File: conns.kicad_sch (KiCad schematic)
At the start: 10 parts, among them J1 GSB1C4621DS1HR, J2 M20-8770546 (for SWD), J3 M20-8770342 (for RasPi), J4 JST-XH, J6 SMA_CONNECTOR, J7 SMA_CONNECTOR

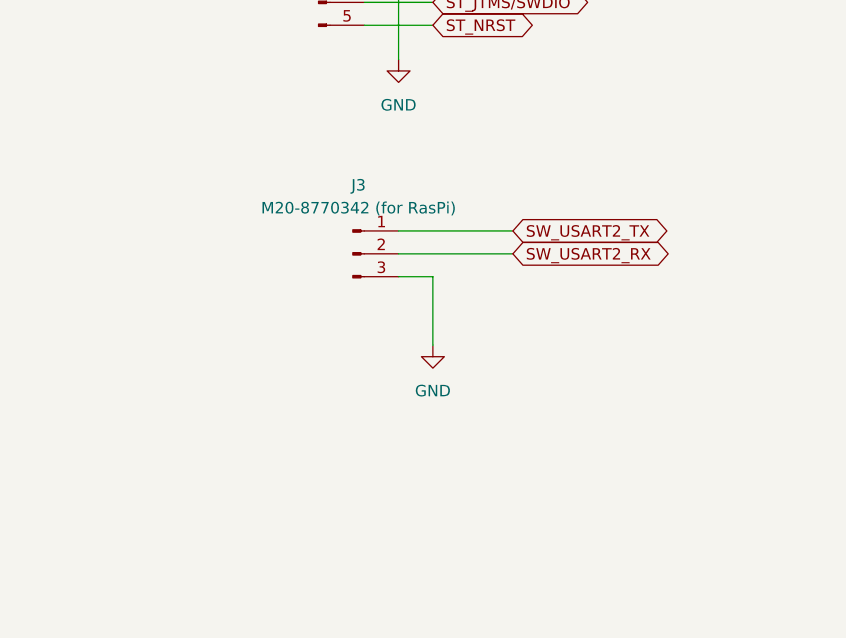
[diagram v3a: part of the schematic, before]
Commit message: adding connectors for display and pi power, pin headers
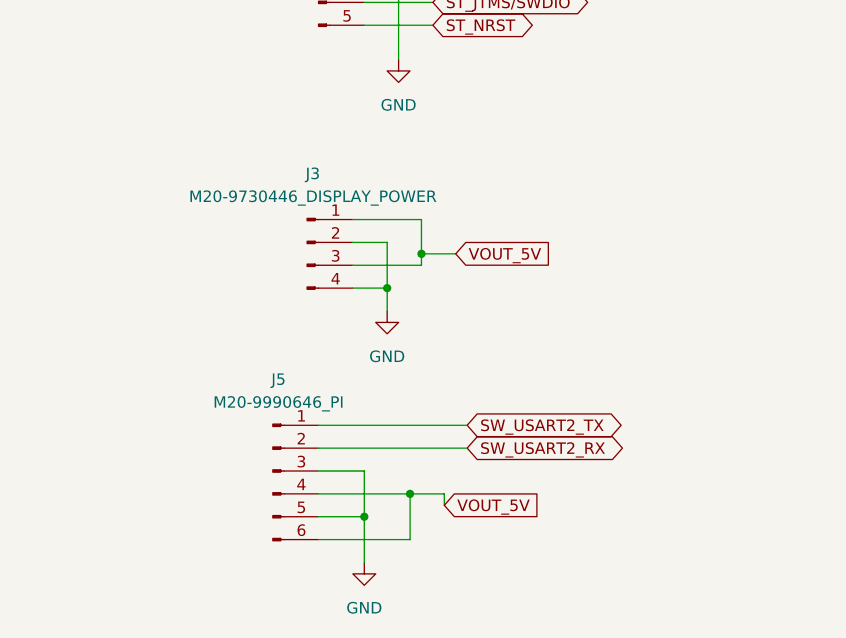
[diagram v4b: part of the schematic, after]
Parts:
- removed J3: M20-8770342 (for RasPi), Connector_PinSocket_2.54mm:PinSocket_1x03_P2.54mm_Vertical, symbol Connector:Conn_01x03_Pin
- added J3: M20-9730446_DISPLAY_POWER, Connector_PinHeader_2.54mm:PinHeader_1x04_P2.54mm_Vertical, symbol Connector:Conn_01x04_Pin
- added J5: M20-9990646_PI, Connector_PinHeader_2.54mm:PinHeader_1x06_P2.54mm_Vertical, symbol Connector:Conn_01x06_Pin
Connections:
- net GND: now also J3.2 (Pin_2), J3.4 (Pin_4), J5.3 (Pin_3), J5.5 (Pin_5)
- net SW_USART2_RX: now also J5.2 (Pin_2)
- net SW_USART2_TX: now also J5.1 (Pin_1)
- new net VOUT_5V: J3.1 (Pin_1), J3.3 (Pin_3), J5.4 (Pin_4), J5.6 (Pin_6)

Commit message: adding the .stp files for 3d viewer
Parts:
- J2: footprint Connector_PinSocket_2.54mm:PinSocket_1x05_P2.54mm_Vertical -> Connector_PinHeader_2.54mm:PinHeader_1x05_P2.54mm_Vertical
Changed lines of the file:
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@@
       (effects (font (size 1.27 1.27)))
     )
-    (property "Footprint" "Connector_PinSocket_2.54mm:PinSocket_1x05_P2.54mm_Vertical" (at 50.8 111.76 0)
+    (property "Footprint" "Connector_PinHeader_2.54mm:PinHeader_1x05_P2.54mm_Vertical" (at 50.8 111.76 0)
       (effects (font (size 1.27 1.27)) hide)
     )

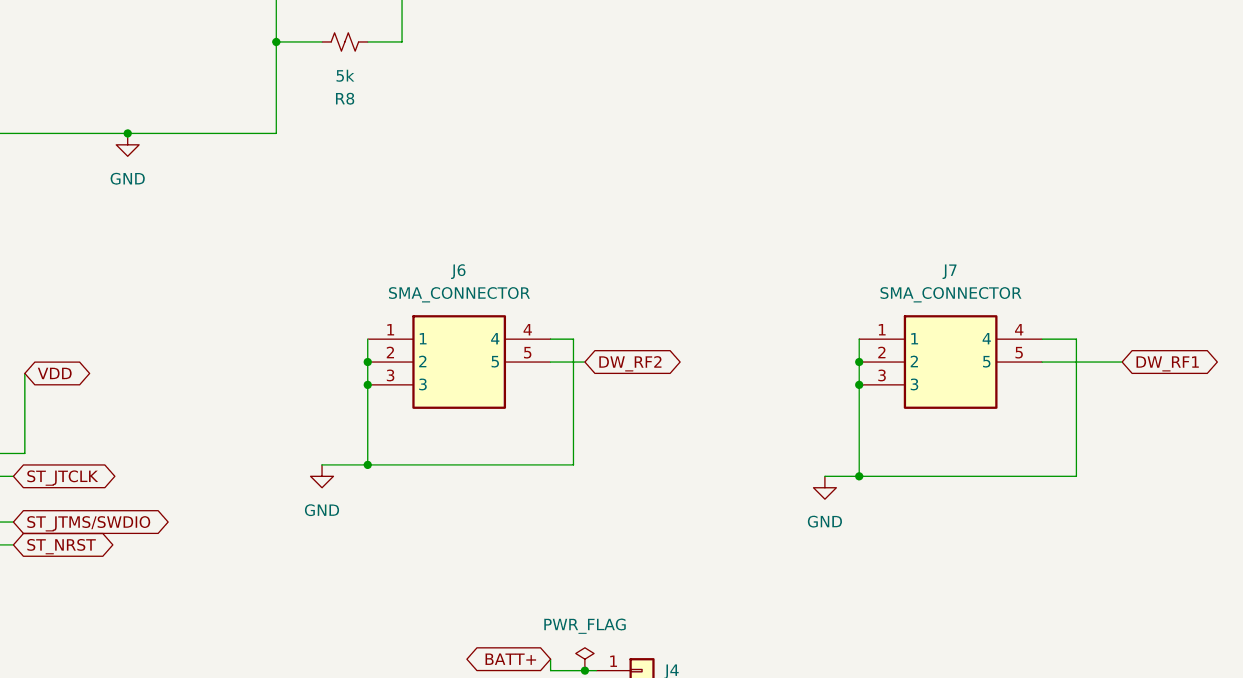
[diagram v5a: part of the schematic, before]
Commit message: routing on rf ic DW3220
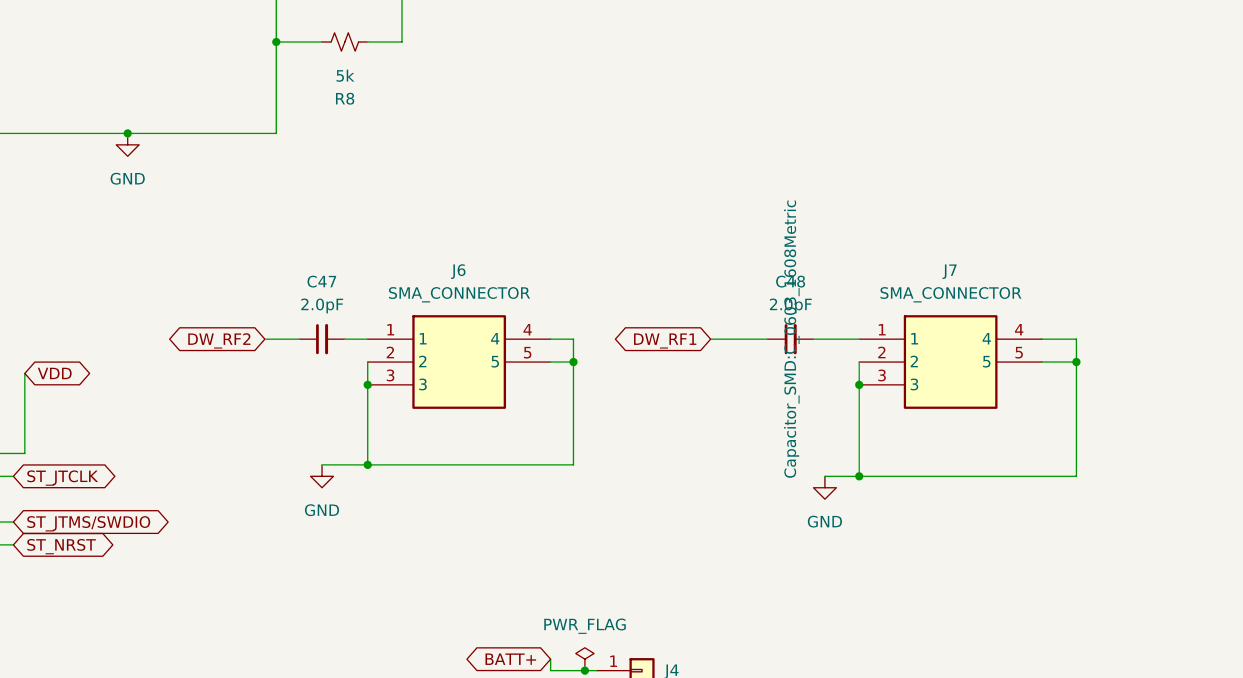
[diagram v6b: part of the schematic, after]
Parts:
- added C47, C48: 2.0pF, Capacitor_SMD:C_0603_1608Metric, symbol Device:C_Small
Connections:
- net DW_RF1: now also C48.1; no longer J7.5
- net DW_RF2: now also C47.1; no longer J6.5
- net GND: now also J6.5, J7.5; no longer J6.1, J7.1
- new net: C47.2, J6.1
- new net: C48.2, J7.1
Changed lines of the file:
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@@
   (junction (at 58.42 146.05) (diameter 0) (color 0 0 0 0)
   )
+  (junction (at 181.61 96.52) (diameter 0) (color 0 0 0 0)
+  )
+  (junction (at 125.73 96.52) (diameter 0) (color 0 0 0 0)
+  )
   (junction (at 92.71 60.96) (diameter 0) (color 0 0 0 0)
   )
   (junction (at 102.87 99.06) (diameter 0) (color 0 0 0 0)
   )
-  (junction (at 102.87 96.52) (diameter 0) (color 0 0 0 0)
-  )
   (junction (at 62.23 142.24) (diameter 0) (color 0 0 0 0)
   )
@@
   )
   (junction (at 92.71 53.34) (diameter 0) (color 0 0 0 0)
-  )
-  (junction (at 157.48 96.52) (diameter 0) (color 0 0 0 0)
   )
   (junction (at 60.96 168.91) (diameter 0) (color 0 0 0 0)
@@
     (stroke (width 0) (type default))
   )
-  (wire (pts (xy 102.87 93.98) (xy 102.87 96.52))
-    (stroke (width 0) (type default))
-  )
-  (wire (pts (xy 123.19 96.52) (xy 127 96.52))
-    (stroke (width 0) (type default))
-  )
   (wire (pts (xy 90.17 53.34) (xy 92.71 53.34))
     (stroke (width 0) (type default))
   )
+  (wire (pts (xy 181.61 96.52) (xy 181.61 109.22))
+    (stroke (width 0) (type default))
+  )
   (wire (pts (xy 62.23 143.51) (xy 62.23 142.24))
     (stroke (width 0) (type default))
   )
+  (wire (pts (xy 123.19 96.52) (xy 125.73 96.52))
+    (stroke (width 0) (type default))
+  )
   (wire (pts (xy 50.8 166.37) (xy 55.88 166.37))
     (stroke (width 0) (type default))
@@
     (stroke (width 0) (type default))
   )
+  (wire (pts (xy 125.73 96.52) (xy 125.73 107.95))
+    (stroke (width 0) (type default))
+  )
   (wire (pts (xy 64.77 106.68) (xy 64.77 97.79))
     (stroke (width 0) (type default))
@@
     (stroke (width 0) (type default))
   )
-  (wire (pts (xy 181.61 93.98) (xy 181.61 109.22))
+  (wire (pts (xy 152.4 93.98) (xy 157.48 93.98))
+    (stroke (width 0) (type default))
+  )
+  (wire (pts (xy 181.61 93.98) (xy 181.61 96.52))
     (stroke (width 0) (type default))
   )
@@
     (stroke (width 0) (type default))
   )
-  (wire (pts (xy 186.69 96.52) (xy 177.8 96.52))
-    (stroke (width 0) (type default))
-  )
   (wire (pts (xy 58.42 140.97) (xy 58.42 146.05))
     (stroke (width 0) (type default))
@@
     (stroke (width 0) (type default))
   )
-  (wire (pts (xy 157.48 93.98) (xy 157.48 96.52))
+  (wire (pts (xy 100.33 93.98) (xy 102.87 93.98))
     (stroke (width 0) (type default))
   )
@@
     (stroke (width 0) (type default))
   )
+  (wire (pts (xy 91.44 93.98) (xy 95.25 93.98))
+    (stroke (width 0) (type default))
+  )
   (wire (pts (xy 39.37 50.8) (xy 39.37 53.34))
     (stroke (width 0) (type default))
@@
     (stroke (width 0) (type default))
   )
+  (wire (pts (xy 140.97 93.98) (xy 147.32 93.98))
+    (stroke (width 0) (type default))
+  )
   (wire (pts (xy 50.8 163.83) (xy 67.31 163.83))
     (stroke (width 0) (type default))
@@
     (stroke (width 0) (type default))
   )
-  (wire (pts (xy 125.73 93.98) (xy 125.73 107.95))
+  (wire (pts (xy 125.73 93.98) (xy 125.73 96.52))
+    (stroke (width 0) (type default))
+  )
+  (wire (pts (xy 177.8 96.52) (xy 181.61 96.52))
     (stroke (width 0) (type default))
   )
@@
     )
   )
+  (global_label "DW_RF2" (shape bidirectional) (at 91.44 93.98 180) (fields_autoplaced)
+    (effects (font (size 1.27 1.27)) (justify right))
+    (property "Intersheetrefs" "${INTERSHEET_REFS}" (at 80.0864 93.98 0)
+      (effects (font (size 1.27 1.27)) (justify right) hide)
+    )
+  )
   (global_label "BATT+" (shape bidirectional) (at 123.19 129.54 180) (fields_autoplaced)
     (effects (font (size 1.27 1.27)) (justify right))
@@
     )
   )
-  (global_label "DW_RF1" (shape bidirectional) (at 186.69 96.52 0) (fields_autoplaced)
-    (effects (font (size 1.27 1.27)) (justify left))
-    (property "Intersheetrefs" "${INTERSHEET_REFS}" (at 198.0436 96.52 0)
-      (effects (font (size 1.27 1.27)) (justify left) hide)
-    )
-  )
   (global_label "ST_JTCLK" (shape bidirectional) (at 63.5 109.22 0) (fields_autoplaced)
     (effects (font (size 1.27 1.27)) (justify left))
@@
     )
   )
+  (global_label "DW_RF1" (shape bidirectional) (at 140.97 93.98 180) (fields_autoplaced)
+    (effects (font (size 1.27 1.27)) (justify right))
+    (property "Intersheetrefs" "${INTERSHEET_REFS}" (at 129.6164 93.98 0)
+      (effects (font (size 1.27 1.27)) (justify right) hide)
+    )
+  )
   (global_label "SW_USART2_RX" (shape bidirectional) (at 67.31 163.83 0) (fields_autoplaced)
     (effects (font (size 1.27 1.27)) (justify left))
@@
     )
   )
-  (global_label "DW_RF2" (shape bidirectional) (at 127 96.52 0) (fields_autoplaced)
-    (effects (font (size 1.27 1.27)) (justify left))
-    (property "Intersheetrefs" "${INTERSHEET_REFS}" (at 138.3536 96.52 0)
-      (effects (font (size 1.27 1.27)) (justify left) hide)
-    )
-  )
   (symbol (lib_id "Connector:Conn_01x06_Pin") (at 45.72 166.37 0) (unit 1)
     (in_bom yes) (on_board yes) (dnp no) (fields_autoplaced)
@@
     )
   )
+  (symbol (lib_id "Device:C_Small") (at 97.79 93.98 90) (unit 1)
+    (in_bom yes) (on_board yes) (dnp no) (fields_autoplaced)
+    (property "Reference" "C47" (at 97.7963 87.63 90)
+      (effects (font (size 1.27 1.27)))
+    )
+    (property "Value" "2.0pF" (at 97.7963 90.17 90)
+      (effects (font (size 1.27 1.27)))
+    )
+    (property "Footprint" "Capacitor_SMD:C_0603_1608Metric" (at 97.79 93.98 0)
+      (effects (font (size 1.27 1.27)) hide)
+    )
+    (property "Datasheet" "~" (at 97.79 93.98 0)
+      (effects (font (size 1.27 1.27)) hide)
+    )
+    (pin "2")
+    (pin "1")
+    (instances
+      (project "radar2"
+        (path "/4b235fed-a05d-46ae-99fd-4a907d865754/dfc10a02-f047-425a-8f9d-e4a822e029f8"
+          (reference "C47") (unit 1)
+        )
+      )
+    )
+  )
   (symbol (lib_id "Connector_Generic:Conn_01x02") (at 133.35 130.81 0) (unit 1)
     (in_bom yes) (on_board yes) (dnp no) (fields_autoplaced)
@@
         )
       )
+    )
+  )
+  (symbol (lib_id "Device:C_Small") (at 149.86 93.98 90) (unit 1)
+    (in_bom yes) (on_board yes) (dnp no) (fields_autoplaced)
+    (property "Reference" "C48" (at 149.8663 87.63 90)
+      (effects (font (size 1.27 1.27)))
+    )
+    (property "Value" "2.0pF" (at 149.8663 90.17 90)
+      (effects (font (size 1.27 1.27)))
+    )
+    (property "Footprint" "Capacitor_SMD:C_0603_1608Metric" (at 149.86 93.98 0)
+      (effects (font (size 1.27 1.27)))
+    )
+    (property "Datasheet" "~" (at 149.86 93.98 0)
+      (effects (font (size 1.27 1.27)) hide)
+    )
+    (pin "2")
+    (pin "1")
+    (instances
+      (project "radar2"
+        (path "/4b235fed-a05d-46ae-99fd-4a907d865754/dfc10a02-f047-425a-8f9d-e4a822e029f8"
+          (reference "C48") (unit 1)
+        )
+      )

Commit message: changing sizes of caps from 06 to 04, also using vias on DW spi interfact to stm32
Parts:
- C47, C48: footprint Capacitor_SMD:C_0603_1608Metric -> Capacitor_SMD:C_0402_1005Metric
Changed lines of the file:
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@@
       (effects (font (size 1.27 1.27)))
     )
-    (property "Footprint" "Capacitor_SMD:C_0603_1608Metric" (at 97.79 93.98 0)
+    (property "Footprint" "Capacitor_SMD:C_0402_1005Metric" (at 97.79 93.98 0)
       (effects (font (size 1.27 1.27)) hide)
     )
@@
   )
   (symbol (lib_id "Connector:Conn_01x04_Pin") (at 49.53 140.97 0) (unit 1)
-    (in_bom yes) (on_board yes) (dnp no) (fields_autoplaced)
+    (in_bom yes) (on_board yes) (dnp no)
     (property "Reference" "J3" (at 50.165 133.35 0)
       (effects (font (size 1.27 1.27)))
@@
   )
   (symbol (lib_id "Device:C_Small") (at 149.86 93.98 90) (unit 1)
-    (in_bom yes) (on_board yes) (dnp no) (fields_autoplaced)
+    (in_bom yes) (on_board yes) (dnp no)
     (property "Reference" "C48" (at 149.8663 87.63 90)
       (effects (font (size 1.27 1.27)))
@@
       (effects (font (size 1.27 1.27)))
     )
-    (property "Footprint" "Capacitor_SMD:C_0603_1608Metric" (at 149.86 93.98 0)
-      (effects (font (size 1.27 1.27)))
+    (property "Footprint" "Capacitor_SMD:C_0402_1005Metric" (at 149.86 81.28 90)
+      (effects (font (size 1.27 1.27)) hide)
     )
     (property "Datasheet" "~" (at 149.86 93.98 0)

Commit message: replacing our indcutr for TPS with proper one, creating a bom tool for easier component selection and fitering, currently getting all my passives in order
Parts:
- C6: value 0.1muF -> 0.1uF
- C7: value 22muF -> 22uF
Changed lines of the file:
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@@
       (effects (font (size 1.27 1.27)) (justify right))
     )
-    (property "Value" "0.1muF" (at 41.91 57.1436 0)
+    (property "Value" "0.1uF" (at 41.91 57.1436 0)
       (effects (font (size 1.27 1.27)) (justify right))
     )
@@
       (effects (font (size 1.27 1.27)) (justify right))
     )
-    (property "Value" "22muF" (at 30.48 57.1436 0)
+    (property "Value" "22uF" (at 30.48 57.1436 0)
       (effects (font (size 1.27 1.27)) (justify right))
     )
